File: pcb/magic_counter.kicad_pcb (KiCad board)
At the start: 2 copper layers, 127.4 x 152.4 mm, 30 parts, among them J1 ISP-Port, Q1 2SA1015, Q2 2SA1015, Q3 2SA1015, Q4 2SA1015, Q5 2SA1015, U1 ATmega32A-P, U2 74HC595, U7 LTC-4627JF, Y1 Crystal

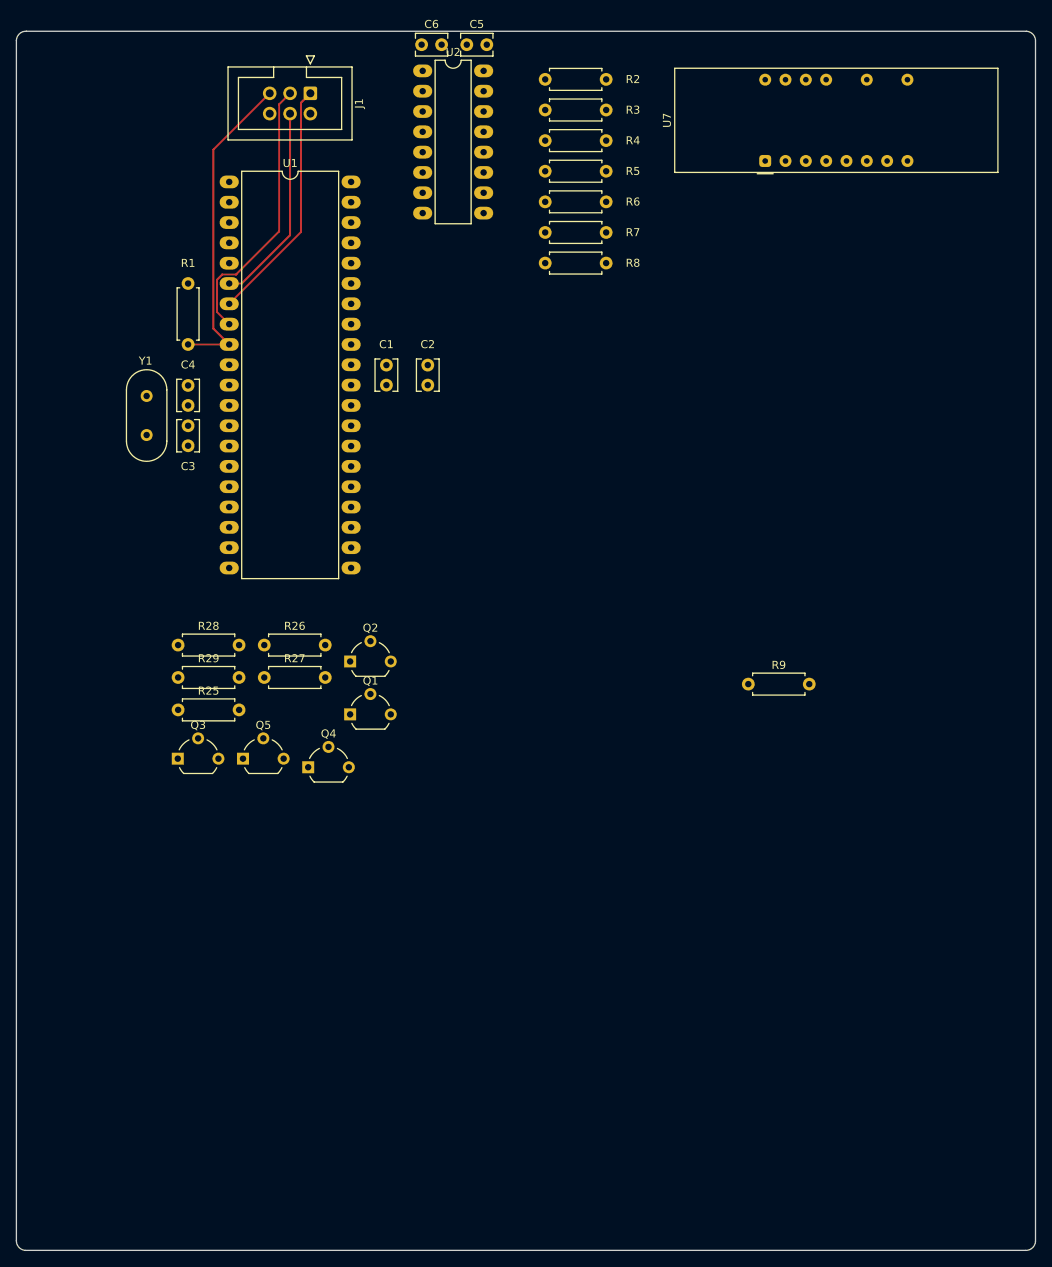
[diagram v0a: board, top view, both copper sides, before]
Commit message: test layout and first traces
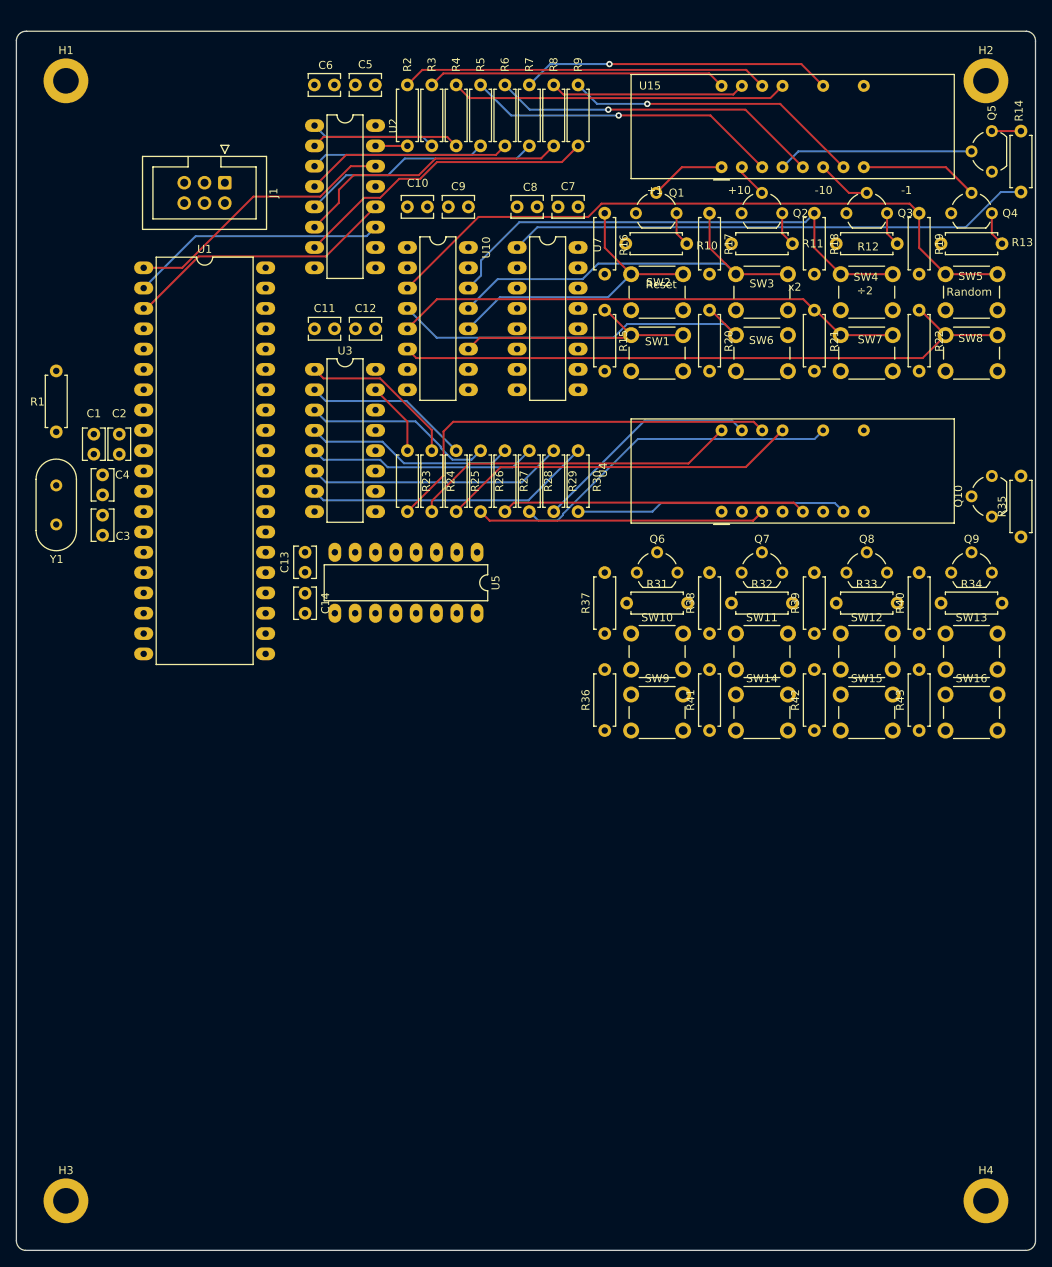
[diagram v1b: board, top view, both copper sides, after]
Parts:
- added C10: 1nF, Capacitor_THT:C_Disc_D3.8mm_W2.6mm_P2.50mm, F.Cu at (83.1, 45.6)
- added C11: 100pF, Capacitor_THT:C_Disc_D3.8mm_W2.6mm_P2.50mm, F.Cu at (69.0, 60.8)
- added C12: 1nF, Capacitor_THT:C_Disc_D3.8mm_W2.6mm_P2.50mm, F.Cu at (74.1, 60.8)
- added C13: 100pF, Capacitor_THT:C_Disc_D3.8mm_W2.6mm_P2.50mm, F.Cu at (67.8, 91.3)
- added C14: 1nF, Capacitor_THT:C_Disc_D3.8mm_W2.6mm_P2.50mm, F.Cu at (67.8, 93.9)
- added C7: 100pF, Capacitor_THT:C_Disc_D3.8mm_W2.6mm_P2.50mm, F.Cu at (99.4, 45.6)
- added C8: 1nF, Capacitor_THT:C_Disc_D3.8mm_W2.6mm_P2.50mm, F.Cu at (96.8, 45.6)
- added C9: 100pF, Capacitor_THT:C_Disc_D3.8mm_W2.6mm_P2.50mm, F.Cu at (85.7, 45.6)
- added H1: MountingHole_Pad, MountingHole:MountingHole_3.2mm_M3_DIN965_Pad, F.Cu at (37.9, 29.8)
- added H2: MountingHole_Pad, MountingHole:MountingHole_3.2mm_M3_DIN965_Pad, F.Cu at (152.9, 29.8)
- added H3: MountingHole_Pad, MountingHole:MountingHole_3.2mm_M3_DIN965_Pad, F.Cu at (37.9, 169.8)
- added H4: MountingHole_Pad, MountingHole:MountingHole_3.2mm_M3_DIN965_Pad, F.Cu at (152.9, 169.8)
- added Q10: 2SA1015, Package_TO_SOT_THT:TO-92_Wide, F.Cu at (153.6, 84.3)
- added Q6: 2SA1015, Package_TO_SOT_THT:TO-92_Wide, F.Cu at (109.2, 91.3)
- added Q7: 2SA1015, Package_TO_SOT_THT:TO-92_Wide, F.Cu at (122.3, 91.3)
- added Q8: 2SA1015, Package_TO_SOT_THT:TO-92_Wide, F.Cu at (135.4, 91.3)
- added Q9: 2SA1015, Package_TO_SOT_THT:TO-92_Wide, F.Cu at (148.6, 91.3)
- added R10: 4.7k, Resistor_THT:R_Axial_DIN0207_L6.3mm_D2.5mm_P7.62mm_Horizontal, F.Cu at (107.9, 50.2)
- added R11: 4.7k, Resistor_THT:R_Axial_DIN0207_L6.3mm_D2.5mm_P7.62mm_Horizontal, F.Cu at (121.1, 50.2)
- added R12: 4.7k, Resistor_THT:R_Axial_DIN0207_L6.3mm_D2.5mm_P7.62mm_Horizontal, F.Cu at (134.2, 50.2)
- added R13: 4.7k, Resistor_THT:R_Axial_DIN0207_L6.3mm_D2.5mm_P7.62mm_Horizontal, F.Cu at (147.3, 50.2)
- added R14: 4.7k, Resistor_THT:R_Axial_DIN0207_L6.3mm_D2.5mm_P7.62mm_Horizontal, F.Cu at (157.3, 43.8)
- added R15: 10k, Resistor_THT:R_Axial_DIN0207_L6.3mm_D2.5mm_P7.62mm_Horizontal, F.Cu at (105.2, 66.1)
- added R16: 10k, Resistor_THT:R_Axial_DIN0207_L6.3mm_D2.5mm_P7.62mm_Horizontal, F.Cu at (105.2, 54.0)
- added R17: 10k, Resistor_THT:R_Axial_DIN0207_L6.3mm_D2.5mm_P7.62mm_Horizontal, F.Cu at (118.3, 54.0)
- added R18: 10k, Resistor_THT:R_Axial_DIN0207_L6.3mm_D2.5mm_P7.62mm_Horizontal, F.Cu at (131.4, 54.0)
- added R19: 10k, Resistor_THT:R_Axial_DIN0207_L6.3mm_D2.5mm_P7.62mm_Horizontal, F.Cu at (144.5, 54.0)
- added R20: 10k, Resistor_THT:R_Axial_DIN0207_L6.3mm_D2.5mm_P7.62mm_Horizontal, F.Cu at (118.3, 66.1)
- added R21: 10k, Resistor_THT:R_Axial_DIN0207_L6.3mm_D2.5mm_P7.62mm_Horizontal, F.Cu at (131.4, 66.1)
- added R22: 10k, Resistor_THT:R_Axial_DIN0207_L6.3mm_D2.5mm_P7.62mm_Horizontal, F.Cu at (144.5, 66.1)
- added R23: 100R, Resistor_THT:R_Axial_DIN0207_L6.3mm_D2.5mm_P7.62mm_Horizontal, F.Cu at (80.6, 76.1)
- added R24: 100R, Resistor_THT:R_Axial_DIN0207_L6.3mm_D2.5mm_P7.62mm_Horizontal, F.Cu at (83.6, 76.1)
- added R30: 100R, Resistor_THT:R_Axial_DIN0207_L6.3mm_D2.5mm_P7.62mm_Horizontal, F.Cu at (101.9, 76.1)
- added R31: 4.7k, Resistor_THT:R_Axial_DIN0207_L6.3mm_D2.5mm_P7.62mm_Horizontal, F.Cu at (108.0, 95.1)
- added R32: 4.7k, Resistor_THT:R_Axial_DIN0207_L6.3mm_D2.5mm_P7.62mm_Horizontal, F.Cu at (121.1, 95.1)
- added R33: 4.7k, Resistor_THT:R_Axial_DIN0207_L6.3mm_D2.5mm_P7.62mm_Horizontal, F.Cu at (134.2, 95.1)
- added R34: 4.7k, Resistor_THT:R_Axial_DIN0207_L6.3mm_D2.5mm_P7.62mm_Horizontal, F.Cu at (147.3, 95.1)
- added R35: 4.7k, Resistor_THT:R_Axial_DIN0207_L6.3mm_D2.5mm_P7.62mm_Horizontal, F.Cu at (157.3, 86.9)
- added R36: 10k, Resistor_THT:R_Axial_DIN0207_L6.3mm_D2.5mm_P7.62mm_Horizontal, F.Cu at (105.2, 111.1)
- added R37: 10k, Resistor_THT:R_Axial_DIN0207_L6.3mm_D2.5mm_P7.62mm_Horizontal, F.Cu at (105.2, 98.9)
- added R38: 10k, Resistor_THT:R_Axial_DIN0207_L6.3mm_D2.5mm_P7.62mm_Horizontal, F.Cu at (118.3, 98.9)
- added R39: 10k, Resistor_THT:R_Axial_DIN0207_L6.3mm_D2.5mm_P7.62mm_Horizontal, F.Cu at (131.4, 98.9)
- added R40: 10k, Resistor_THT:R_Axial_DIN0207_L6.3mm_D2.5mm_P7.62mm_Horizontal, F.Cu at (144.5, 98.9)
- added R41: 10k, Resistor_THT:R_Axial_DIN0207_L6.3mm_D2.5mm_P7.62mm_Horizontal, F.Cu at (118.3, 111.1)
- added R42: 10k, Resistor_THT:R_Axial_DIN0207_L6.3mm_D2.5mm_P7.62mm_Horizontal, F.Cu at (131.4, 111.1)
- added R43: 10k, Resistor_THT:R_Axial_DIN0207_L6.3mm_D2.5mm_P7.62mm_Horizontal, F.Cu at (144.5, 111.1)
- added SW1: Reset, Button_Switch_THT:SW_PUSH_6mm_H5mm, F.Cu at (108.5, 61.6)
- added SW10: +1, Button_Switch_THT:SW_PUSH_6mm_H5mm, F.Cu at (108.5, 98.9)
- added SW11: +10, Button_Switch_THT:SW_PUSH_6mm_H5mm, F.Cu at (121.6, 98.9)
- added SW12: -10, Button_Switch_THT:SW_PUSH_6mm_H5mm, F.Cu at (134.7, 98.9)
- added SW13: -1, Button_Switch_THT:SW_PUSH_6mm_H5mm, F.Cu at (147.8, 98.9)
- added SW14: x2, Button_Switch_THT:SW_PUSH_6mm_H5mm, F.Cu at (121.6, 106.6)
- added SW15: /2, Button_Switch_THT:SW_PUSH_6mm_H5mm, F.Cu at (134.7, 106.6)
- added SW16: Random, Button_Switch_THT:SW_PUSH_6mm_H5mm, F.Cu at (147.8, 106.6)
- added SW2: +1, Button_Switch_THT:SW_PUSH_6mm_H5mm, F.Cu at (108.5, 54.0)
- added SW3: +10, Button_Switch_THT:SW_PUSH_6mm_H5mm, F.Cu at (121.6, 54.0)
- added SW4: -10, Button_Switch_THT:SW_PUSH_6mm_H5mm, F.Cu at (134.7, 54.0)
- added SW5: -1, Button_Switch_THT:SW_PUSH_6mm_H5mm, F.Cu at (147.8, 54.0)
- added SW6: x2, Button_Switch_THT:SW_PUSH_6mm_H5mm, F.Cu at (121.6, 61.6)
- added SW7: /2, Button_Switch_THT:SW_PUSH_6mm_H5mm, F.Cu at (134.7, 61.6)
- added SW8: Random, Button_Switch_THT:SW_PUSH_6mm_H5mm, F.Cu at (147.8, 61.6)
- added SW9: Reset, Button_Switch_THT:SW_PUSH_6mm_H5mm, F.Cu at (108.5, 106.6)
- added U10: 74HC165, Package_DIP:DIP-16_W7.62mm_LongPads, F.Cu at (80.6, 50.7)
- added U15: LTC-4627JF, Display_7Segment:LTC-4627Jx, F.Cu at (119.8, 40.6)
- added U3: 74HC595, Package_DIP:DIP-16_W7.62mm_LongPads, F.Cu at (69.0, 65.9)
- added U4: LTC-4627JF, Display_7Segment:LTC-4627Jx, F.Cu at (119.8, 83.7)
- added U5: 74HC165, Package_DIP:DIP-16_W7.62mm_LongPads, F.Cu at (89.3, 88.8)
- R25, R26, R27, R28, R29: value 4.7k -> 100R
- U7: value LTC-4627JF -> 4028; footprint Display_7Segment:LTC-4627Jx -> Package_DIP:DIP-16_W7.62mm_LongPads
- moved Q5 118.9 mm to (153.6, 41.2), turned to 90 degrees
- moved Q3 107.9 mm to (135.4, 46.4)
- moved Q4 106.1 mm to (148.6, 46.4)
- moved Q2 74.4 mm to (122.3, 46.4)
- moved Q1 72.1 mm to (109.1, 46.4)
- moved R9 70.6 mm to (101.9, 38.0), turned to 90 degrees
- moved R29 54.8 mm to (98.9, 76.1), turned to -90 degrees
- moved R28 50.2 mm to (95.8, 76.1), turned to -90 degrees
- moved R25 47.5 mm to (86.7, 76.1), turned to -90 degrees
- moved R27 41.3 mm to (92.8, 76.1), turned to -90 degrees
- moved C2 39.5 mm to (44.6, 76.5)
- moved C1 37.6 mm to (41.4, 76.5)
- moved R26 36.4 mm to (89.7, 76.1), turned to -90 degrees
- moved U7 32.8 mm to (94.3, 50.7), turned to 0 degrees
- moved R2 19.1 mm to (80.6, 38.0), turned to 90 degrees
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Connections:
- R25 pad 1: unconnected-(R25-Pad1) -> Net-(R25-Pad1)
- R25 pad 2: Net-(Q1-Pad3) -> Net-(R25-Pad2)
- R26 pad 1: unconnected-(R26-Pad1) -> Net-(R26-Pad1)
- R26 pad 2: Net-(Q2-Pad3) -> Net-(R26-Pad2)
- R27 pad 1: unconnected-(R27-Pad1) -> Net-(R27-Pad1)
- R27 pad 2: Net-(Q3-Pad3) -> Net-(R27-Pad2)
- R28 pad 1: unconnected-(R28-Pad1) -> Net-(R28-Pad1)
- R28 pad 2: Net-(Q4-Pad3) -> Net-(R28-Pad2)
- R29 pad 1: unconnected-(R29-Pad1) -> Net-(R29-Pad1)
- R29 pad 2: Net-(Q5-Pad3) -> Net-(R29-Pad2)
- U1 pad 1: unconnected-(U1-Pad1) -> /PB1
- U1 pad 14: unconnected-(U1-Pad14) -> /PD0
- U1 pad 15: unconnected-(U1-Pad15) -> /PD1
- U1 pad 16: unconnected-(U1-Pad16) -> /PD2
- U1 pad 17: unconnected-(U1-Pad17) -> /PD3
- U1 pad 2: unconnected-(U1-Pad2) -> /PB2
- U1 pad 3: unconnected-(U1-Pad3) -> /PB3
- U1 pad 37: unconnected-(U1-Pad37) -> /PA3
- U1 pad 38: unconnected-(U1-Pad38) -> /PA2
- U1 pad 39: unconnected-(U1-Pad39) -> /PA1
- U1 pad 40: unconnected-(U1-Pad40) -> /PA0
- U2 pad 10: unconnected-(U2-Pad10) -> +5V
- U2 pad 11: unconnected-(U2-Pad11) -> /PB2
- U2 pad 12: unconnected-(U2-Pad12) -> /PB3
- U2 pad 13: unconnected-(U2-Pad13) -> GND
- U2 pad 14: unconnected-(U2-Pad14) -> /PB1
- U2 pad 9: unconnected-(U2-Pad9) -> /Display_life/2nd_Bitshifter
- U7 pad 1: Net-(Q1-Pad2) -> /Display_life/D1_CA5
- U7 pad 11: Net-(R7-Pad2) -> /PA3
- U7 pad 13: Net-(R4-Pad2) -> /PA1
- U7 pad 14: Net-(R2-Pad2) -> /Display_life/D1_CA2
- U7 pad 15: Net-(R8-Pad2) -> /Display_life/D1_CA4
- U7 pad 16: Net-(R3-Pad2) -> +5V
- U7 pad 2: Net-(Q2-Pad2) -> /Display_life/D1_CA3
- U7 pad 3: Net-(R5-Pad2) -> /Display_life/D1_CA1
- U7 pad 4: Net-(Q5-Pad2) -> /Display_life/D2_CA3
- U7 pad 5: Net-(R6-Pad2) -> /Display_life/D2_CA5
- U7 pad 6: Net-(Q3-Pad2) -> /Display_life/D2_CA1
- U7 pad 7: Net-(R9-Pad2) -> /Display_life/D2_CA2
- U7 pad 8: Net-(Q4-Pad2) -> GND
- U7 pad 9: unconnected-(U7-Pad9) -> /Display_life/D2_CA4
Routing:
- net Net-(R19-Pad2): track 0.00 -> 84.3 mm
- net Net-(R22-Pad2): track 0.00 -> 80.0 mm
- net /Display_life/D1_CA5: track 0.00 -> 65.9 mm
- net Net-(R21-Pad2): track 0.00 -> 64.1 mm
- net Net-(R18-Pad2): track 0.00 -> 63.7 mm
- net Net-(R23-Pad2): track 0.00 -> 52.7 mm
- net Net-(R17-Pad2): track 0.00 -> 51.8 mm
- net Net-(R20-Pad2): track 0.00 -> 48.5 mm
- net Net-(R2-Pad2): track 0.00 -> 46.0 mm
- net Net-(R25-Pad2): track 0.00 -> 45.0 mm
- net Net-(R4-Pad2): track 0.00 -> 42.1 mm
- net Net-(R28-Pad2): track 0.00 -> 42.0 mm
- net Net-(R6-Pad2): track 0.00 -> 41.5 mm, vias 0 -> 1
- net Net-(R24-Pad2): track 0.00 -> 41.2 mm
- net /Reset: track 40.3 -> 0.00 mm
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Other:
- board text added: "+1"
- board text added: "+10"
- board text added: "-1"
- board text added: "-10"
- board text added: "Random"
- board text added: "Reset"
- board text added: "x2"
- board text added: "÷2"

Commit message: new layout test
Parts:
- added C15: ~, Capacitor_THT:C_Disc_D3.8mm_W2.6mm_P2.50mm, F.Cu at (439.0, 172.1)
- added C16: ~, Capacitor_THT:C_Disc_D3.8mm_W2.6mm_P2.50mm, F.Cu at (449.6, 163.5)
- added C17: ~, Capacitor_THT:C_Disc_D3.8mm_W2.6mm_P2.50mm, F.Cu at (417.5, 197.7)
- added C18: ~, Capacitor_THT:C_Disc_D3.8mm_W2.6mm_P2.50mm, F.Cu at (396.2, 204.9)
- added C19: 100pF, Capacitor_THT:C_Disc_D3.8mm_W2.6mm_P2.50mm, F.Cu at (440.8, 112.8)
- added C20: 1nF, Capacitor_THT:C_Disc_D3.8mm_W2.6mm_P2.50mm, F.Cu at (433.1, 119.4)
- added C21: 100pF, Capacitor_THT:C_Disc_D3.8mm_W2.6mm_P2.50mm, F.Cu at (448.9, 102.2)
- added C22: 1nF, Capacitor_THT:C_Disc_D3.8mm_W2.6mm_P2.50mm, F.Cu at (427.5, 123.6)
- added C23: 100pF, Capacitor_THT:C_Disc_D3.8mm_W2.6mm_P2.50mm, F.Cu at (421.8, 118.4)
- added C24: 1nF, Capacitor_THT:C_Disc_D3.8mm_W2.6mm_P2.50mm, F.Cu at (427.5, 119.4)
- added Q11: 2SA1015, Package_TO_SOT_THT:TO-92_Wide, F.Cu at (419.3, 132.7)
- added Q12: 2SA1015, Package_TO_SOT_THT:TO-92_Wide, F.Cu at (409.4, 140.8)
- added Q13: 2SA1015, Package_TO_SOT_THT:TO-92_Wide, F.Cu at (408.5, 134.2)
- added Q14: 2SA1015, Package_TO_SOT_THT:TO-92_Wide, F.Cu at (432.6, 108.2)
- added Q15: 2SA1015, Package_TO_SOT_THT:TO-92_Wide, F.Cu at (419.3, 126.1)
- added Q16: 2SA1015, Package_TO_SOT_THT:TO-92_Wide, F.Cu at (398.6, 150.4)
- added Q17: 2SA1015, Package_TO_SOT_THT:TO-92_Wide, F.Cu at (401.3, 142.3)
- added Q18: 2SA1015, Package_TO_SOT_THT:TO-92_Wide, F.Cu at (432.6, 114.8)
- added Q19: 2SA1015, Package_TO_SOT_THT:TO-92_Wide, F.Cu at (440.7, 108.2)
- added Q20: 2SA1015, Package_TO_SOT_THT:TO-92_Wide, F.Cu at (390.5, 150.4)
- added R44: 10k, Resistor_THT:R_Axial_DIN0207_L6.3mm_D2.5mm_P7.62mm_Horizontal, F.Cu at (385.6, 163.5)
- added R45: 10k, Resistor_THT:R_Axial_DIN0207_L6.3mm_D2.5mm_P7.62mm_Horizontal, F.Cu at (385.6, 167.5)
- added R46: 10k, Resistor_THT:R_Axial_DIN0207_L6.3mm_D2.5mm_P7.62mm_Horizontal, F.Cu at (385.6, 183.7)
- added R47: 10k, Resistor_THT:R_Axial_DIN0207_L6.3mm_D2.5mm_P7.62mm_Horizontal, F.Cu at (385.6, 179.7)
- added R48: 10k, Resistor_THT:R_Axial_DIN0207_L6.3mm_D2.5mm_P7.62mm_Horizontal, F.Cu at (396.4, 171.6)
- added R49: 10k, Resistor_THT:R_Axial_DIN0207_L6.3mm_D2.5mm_P7.62mm_Horizontal, F.Cu at (396.4, 179.7)
- added R50: 10k, Resistor_THT:R_Axial_DIN0207_L6.3mm_D2.5mm_P7.62mm_Horizontal, F.Cu at (407.2, 171.6)
- added R51: 10k, Resistor_THT:R_Axial_DIN0207_L6.3mm_D2.5mm_P7.62mm_Horizontal, F.Cu at (385.6, 175.6)
- added R52: 10k, Resistor_THT:R_Axial_DIN0207_L6.3mm_D2.5mm_P7.62mm_Horizontal, F.Cu at (396.4, 167.5)
- added R53: 10k, Resistor_THT:R_Axial_DIN0207_L6.3mm_D2.5mm_P7.62mm_Horizontal, F.Cu at (407.2, 163.5)
- added R54: 10k, Resistor_THT:R_Axial_DIN0207_L6.3mm_D2.5mm_P7.62mm_Horizontal, F.Cu at (396.4, 183.7)
- added R55: 10k, Resistor_THT:R_Axial_DIN0207_L6.3mm_D2.5mm_P7.62mm_Horizontal, F.Cu at (396.4, 163.5)
- added R56: 10k, Resistor_THT:R_Axial_DIN0207_L6.3mm_D2.5mm_P7.62mm_Horizontal, F.Cu at (385.6, 171.6)
- added R57: 10k, Resistor_THT:R_Axial_DIN0207_L6.3mm_D2.5mm_P7.62mm_Horizontal, F.Cu at (385.6, 187.8)
- added R58: 10k, Resistor_THT:R_Axial_DIN0207_L6.3mm_D2.5mm_P7.62mm_Horizontal, F.Cu at (396.4, 175.6)
- added R59: 10k, Resistor_THT:R_Axial_DIN0207_L6.3mm_D2.5mm_P7.62mm_Horizontal, F.Cu at (407.2, 167.5)
- added R60: 4.7k, Resistor_THT:R_Axial_DIN0207_L6.3mm_D2.5mm_P7.62mm_Horizontal, F.Cu at (369.0, 143.8)
- added R61: 4.7k, Resistor_THT:R_Axial_DIN0207_L6.3mm_D2.5mm_P7.62mm_Horizontal, F.Cu at (358.2, 143.8)
- added R62: 4.7k, Resistor_THT:R_Axial_DIN0207_L6.3mm_D2.5mm_P7.62mm_Horizontal, F.Cu at (397.8, 136.2)
- added R63: 4.7k, Resistor_THT:R_Axial_DIN0207_L6.3mm_D2.5mm_P7.62mm_Horizontal, F.Cu at (397.8, 128.1)
- added R64: 4.7k, Resistor_THT:R_Axial_DIN0207_L6.3mm_D2.5mm_P7.62mm_Horizontal, F.Cu at (387.0, 132.1)
- added R65: 4.7k, Resistor_THT:R_Axial_DIN0207_L6.3mm_D2.5mm_P7.62mm_Horizontal, F.Cu at (421.8, 102.1)
- added R66: 4.7k, Resistor_THT:R_Axial_DIN0207_L6.3mm_D2.5mm_P7.62mm_Horizontal, F.Cu at (379.8, 147.9)
- added R67: 100R, Resistor_THT:R_Axial_DIN0207_L6.3mm_D2.5mm_P7.62mm_Horizontal, F.Cu at (432.6, 102.1)
- added R68: 100R, Resistor_THT:R_Axial_DIN0207_L6.3mm_D2.5mm_P7.62mm_Horizontal, F.Cu at (369.0, 151.9)
- added R69: 100R, Resistor_THT:R_Axial_DIN0207_L6.3mm_D2.5mm_P7.62mm_Horizontal, F.Cu at (421.8, 114.3)
- added R70: 100R, Resistor_THT:R_Axial_DIN0207_L6.3mm_D2.5mm_P7.62mm_Horizontal, F.Cu at (387.0, 136.2)
- added R71: 100R, Resistor_THT:R_Axial_DIN0207_L6.3mm_D2.5mm_P7.62mm_Horizontal, F.Cu at (358.2, 151.9)
- added R72: 4.7k, Resistor_THT:R_Axial_DIN0207_L6.3mm_D2.5mm_P7.62mm_Horizontal, F.Cu at (408.6, 124.0)
- added R73: 100R, Resistor_THT:R_Axial_DIN0207_L6.3mm_D2.5mm_P7.62mm_Horizontal, F.Cu at (421.8, 110.2)
- added R74: 100R, Resistor_THT:R_Axial_DIN0207_L6.3mm_D2.5mm_P7.62mm_Horizontal, F.Cu at (397.8, 132.1)
- added R75: 100R, Resistor_THT:R_Axial_DIN0207_L6.3mm_D2.5mm_P7.62mm_Horizontal, F.Cu at (387.0, 124.0)
- added R76: 4.7k, Resistor_THT:R_Axial_DIN0207_L6.3mm_D2.5mm_P7.62mm_Horizontal, F.Cu at (390.5, 144.3)
- added R77: 4.7k, Resistor_THT:R_Axial_DIN0207_L6.3mm_D2.5mm_P7.62mm_Horizontal, F.Cu at (369.0, 147.9)
- added R78: 100R, Resistor_THT:R_Axial_DIN0207_L6.3mm_D2.5mm_P7.62mm_Horizontal, F.Cu at (379.8, 151.9)
- added R79: 100R, Resistor_THT:R_Axial_DIN0207_L6.3mm_D2.5mm_P7.62mm_Horizontal, F.Cu at (358.2, 147.9)
- added R80: 100R, Resistor_THT:R_Axial_DIN0207_L6.3mm_D2.5mm_P7.62mm_Horizontal, F.Cu at (390.5, 140.2)
- added R81: 100R, Resistor_THT:R_Axial_DIN0207_L6.3mm_D2.5mm_P7.62mm_Horizontal, F.Cu at (408.6, 128.1)
- added R82: 100R, Resistor_THT:R_Axial_DIN0207_L6.3mm_D2.5mm_P7.62mm_Horizontal, F.Cu at (397.8, 124.0)
- added R83: 100R, Resistor_THT:R_Axial_DIN0207_L6.3mm_D2.5mm_P7.62mm_Horizontal, F.Cu at (387.0, 128.1)
- added R84: 100R, Resistor_THT:R_Axial_DIN0207_L6.3mm_D2.5mm_P7.62mm_Horizontal, F.Cu at (379.8, 143.8)
- added R85: 100R, Resistor_THT:R_Axial_DIN0207_L6.3mm_D2.5mm_P7.62mm_Horizontal, F.Cu at (421.8, 106.2)
- added SW17: ~, Button_Switch_THT:SW_PUSH_6mm_H5mm, F.Cu at (418.4, 163.5)
- added SW18: ~, Button_Switch_THT:SW_PUSH_6mm_H5mm, F.Cu at (428.9, 163.5)
- added SW19: ~, Button_Switch_THT:SW_PUSH_6mm_H5mm, F.Cu at (418.4, 172.0)
- added SW20: ~, Button_Switch_THT:SW_PUSH_6mm_H5mm, F.Cu at (407.2, 201.3)
- added SW21: ~, Button_Switch_THT:SW_PUSH_6mm_H5mm, F.Cu at (407.6, 184.2)
- added SW22: ~, Button_Switch_THT:SW_PUSH_6mm_H5mm, F.Cu at (439.5, 163.5)
- added SW23: ~, Button_Switch_THT:SW_PUSH_6mm_H5mm, F.Cu at (407.4, 192.7)
- added SW24: ~, Button_Switch_THT:SW_PUSH_6mm_H5mm, F.Cu at (386.1, 191.8)
- added SW25: ~, Button_Switch_THT:SW_PUSH_6mm_H5mm, F.Cu at (428.9, 172.0)
- added SW26: ~, Button_Switch_THT:SW_PUSH_6mm_H5mm, F.Cu at (396.6, 196.3)
- added SW27: ~, Button_Switch_THT:SW_PUSH_6mm_H5mm, F.Cu at (428.7, 180.6)
- added SW28: ~, Button_Switch_THT:SW_PUSH_6mm_H5mm, F.Cu at (396.8, 187.8)
- added SW29: ~, Button_Switch_THT:SW_PUSH_6mm_H5mm, F.Cu at (418.2, 180.6)
- added SW30: ~, Button_Switch_THT:SW_PUSH_6mm_H5mm, F.Cu at (418.2, 189.1)
- added SW31: ~, Button_Switch_THT:SW_PUSH_6mm_H5mm, F.Cu at (386.1, 200.4)
- added SW32: ~, Button_Switch_THT:SW_PUSH_6mm_H5mm, F.Cu at (407.6, 175.6)
- added U11: 4028, Package_DIP:DIP-16_W7.62mm_LongPads, F.Cu at (399.0, 102.2)
- added U12: LTC-4627JF, Display_7Segment:LTC-4627Jx, F.Cu at (358.8, 112.1)
- added U13: LTC-4627JF, Display_7Segment:LTC-4627Jx, F.Cu at (410.6, 102.2)
- added U14: ~, Package_DIP:DIP-16_W7.62mm_LongPads, F.Cu at (373.2, 112.1)
- added U6: LTC-4627JF, Display_7Segment:LTC-4627Jx, F.Cu at (55.3, 88.9)
- added U8: 74HC165, Package_DIP:DIP-16_W7.62mm_LongPads, F.Cu at (201.2, 58.9)
- added U9: 74HC595, Package_DIP:DIP-16_W7.62mm_LongPads, F.Cu at (387.4, 102.2)
- U10: value 74HC165 -> 74HC595
- U15: value LTC-4627JF -> ~; footprint Display_7Segment:LTC-4627Jx -> Package_DIP:DIP-16_W7.62mm_LongPads
- U4: value LTC-4627JF -> 4028; footprint Display_7Segment:LTC-4627Jx -> Package_DIP:DIP-16_W7.62mm_LongPads
- U5: value 74HC165 -> LTC-4627JF; footprint Package_DIP:DIP-16_W7.62mm_LongPads -> Display_7Segment:LTC-4627Jx
- U7: value 4028 -> 74HC165
- moved U15 389.6 mm to (492.5, 154.2)
- moved U10 306.9 mm to (383.2, -0.31)
- moved C13 306.9 mm to (370.4, 40.3)
- moved C14 306.9 mm to (370.4, 42.9)
- moved R40 141.1 mm to (275.3, 151.9)
- moved SW13 123.7 mm to (263.1, 143.8)
- moved SW14 123.7 mm to (236.9, 151.5)
- moved R41 123.7 mm to (233.6, 156.0)
- moved R42 123.7 mm to (246.7, 156.0)
- moved R43 123.7 mm to (259.8, 156.0)
- moved SW15 123.7 mm to (250.0, 151.5)
- moved SW16 123.7 mm to (263.1, 151.5)
- moved SW5 110.3 mm to (37.6, 59.4)
- moved Y1 105.0 mm to (130.6, 127.4), turned to 90 degrees
- moved R19 97.9 mm to (47.5, 67.0)
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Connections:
- U1 pad 33: unconnected-(U1-Pad33) -> /PA7
- U1 pad 34: unconnected-(U1-Pad34) -> /PA6
- U1 pad 35: unconnected-(U1-Pad35) -> /PA5
- U1 pad 36: unconnected-(U1-Pad36) -> /PA4
- U10 pad 1: /PD1 -> Net-(R79-Pad1)
- U10 pad 10: /Buttons/Serial_2 -> +5V
- U10 pad 11: Net-(R15-Pad2) -> /PB2
- U10 pad 12: Net-(R16-Pad2) -> /PB3
- U10 pad 13: Net-(R17-Pad2) -> GND
- U10 pad 14: Net-(R18-Pad2) -> /Display_3_and_4/4th_Bitshifter
- U10 pad 15: /PD2 -> Net-(R78-Pad1)
- U10 pad 2: /PD0 -> Net-(R80-Pad1)
- U10 pad 3: Net-(R19-Pad2) -> Net-(R81-Pad1)
- U10 pad 4: Net-(R20-Pad2) -> Net-(R82-Pad1)
- U10 pad 5: Net-(R21-Pad2) -> Net-(R83-Pad1)
- U10 pad 6: Net-(R22-Pad2) -> Net-(R84-Pad1)
- U10 pad 7: GND -> Net-(R85-Pad1)
- U10 pad 9: /PD3 -> unconnected-(U10-Pad9)
- U15 pad 1: Net-(Q1-Pad2) -> /PD1
- U15 pad 11: Net-(R7-Pad2) -> Net-(R52-Pad2)
- U15 pad 13: Net-(R4-Pad2) -> Net-(R54-Pad2)
- U15 pad 14: Net-(R2-Pad2) -> Net-(R55-Pad2)
- U15 pad 15: Net-(R8-Pad2) -> /PD2
- U15 pad 16: Net-(R3-Pad2) -> +5V
- U15 pad 2: Net-(Q2-Pad2) -> /PD0
- U15 pad 3: Net-(R5-Pad2) -> Net-(R56-Pad2)
- U15 pad 4: Net-(Q5-Pad2) -> Net-(R57-Pad2)
- U15 pad 5: Net-(R6-Pad2) -> Net-(R58-Pad2)
- U15 pad 6: Net-(Q3-Pad2) -> Net-(R59-Pad2)
- U15 pad 7: Net-(R9-Pad2) -> GND
- U15 pad 8: Net-(Q4-Pad2) -> GND
- U15 pad 9: unconnected-(U15-Pad9) -> /Buttons_Row_3_and_4/Serial_4
- U3 pad 9: /Display_life/3rd_Bitshifter -> /next_bitshifter
- U4 pad 1: Net-(Q6-Pad2) -> /Display_life/D1_CA5
- U4 pad 11: Net-(R28-Pad2) -> /PA3
- U4 pad 13: Net-(R25-Pad2) -> /PA1
- U4 pad 14: Net-(R23-Pad2) -> /Display_life/D1_CA2
- U4 pad 15: Net-(R29-Pad2) -> /Display_life/D1_CA4
- U4 pad 16: Net-(R24-Pad2) -> +5V
- U4 pad 2: Net-(Q7-Pad2) -> /Display_life/D1_CA3
- U4 pad 3: Net-(R26-Pad2) -> /Display_life/D1_CA1
- U4 pad 4: Net-(Q10-Pad2) -> /Display_life/D2_CA3
- U4 pad 5: Net-(R27-Pad2) -> /Display_life/D2_CA5
- U4 pad 6: Net-(Q8-Pad2) -> /Display_life/D2_CA1
- U4 pad 7: Net-(R30-Pad2) -> /Display_life/D2_CA2
- U4 pad 8: Net-(Q9-Pad2) -> GND
- U4 pad 9: unconnected-(U4-Pad9) -> /Display_life/D2_CA4
- U5 pad 1: /PD1 -> Net-(Q1-Pad2)
- U5 pad 11: Net-(R36-Pad2) -> Net-(R7-Pad2)
- U5 pad 13: Net-(R38-Pad2) -> Net-(R4-Pad2)
- U5 pad 14: Net-(R39-Pad2) -> Net-(R2-Pad2)
- U5 pad 15: /PD2 -> Net-(R8-Pad2)
- U5 pad 16: +5V -> Net-(R3-Pad2)
- U5 pad 2: /PD0 -> Net-(Q2-Pad2)
- U5 pad 3: Net-(R40-Pad2) -> Net-(R5-Pad2)
- U5 pad 4: Net-(R41-Pad2) -> Net-(Q5-Pad2)
- U5 pad 5: Net-(R42-Pad2) -> Net-(R6-Pad2)
- U5 pad 6: Net-(R43-Pad2) -> Net-(Q3-Pad2)
- U5 pad 7: GND -> Net-(R9-Pad2)
- U5 pad 8: GND -> Net-(Q4-Pad2)
- U5 pad 9: /Buttons/Serial_2 -> unconnected-(U5-Pad9)
- U7 pad 1: /Display_life/D1_CA5 -> /PD1
- U7 pad 10: /PA0 -> /Buttons_Row_1_and_2/Serial_2
- U7 pad 11: /PA3 -> Net-(R15-Pad2)
- U7 pad 12: /PA2 -> Net-(R16-Pad2)
- U7 pad 13: /PA1 -> Net-(R17-Pad2)
- U7 pad 14: /Display_life/D1_CA2 -> Net-(R18-Pad2)
- U7 pad 15: /Display_life/D1_CA4 -> /PD2
- U7 pad 2: /Display_life/D1_CA3 -> /PD0
- U7 pad 3: /Display_life/D1_CA1 -> Net-(R19-Pad2)
- U7 pad 4: /Display_life/D2_CA3 -> Net-(R20-Pad2)
- U7 pad 5: /Display_life/D2_CA5 -> Net-(R21-Pad2)
- U7 pad 6: /Display_life/D2_CA1 -> Net-(R22-Pad2)
- U7 pad 7: /Display_life/D2_CA2 -> GND
- U7 pad 9: /Display_life/D2_CA4 -> /PD3
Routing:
- net Net-(R19-Pad2): track 84.3 -> 0.00 mm
- net Net-(R22-Pad2): track 80.0 -> 0.00 mm
- net /Display_life/D1_CA5: track 65.9 -> 0.00 mm
- net Net-(R21-Pad2): track 64.1 -> 0.00 mm
- net Net-(R18-Pad2): track 63.7 -> 0.00 mm
- net Net-(R23-Pad2): track 52.7 -> 0.00 mm
- net Net-(R17-Pad2): track 51.8 -> 0.00 mm
- net Net-(R20-Pad2): track 48.5 -> 0.00 mm
- net Net-(R2-Pad2): track 46.0 -> 0.00 mm
- net Net-(R25-Pad2): track 45.0 -> 0.00 mm
- net Net-(R4-Pad2): track 42.1 -> 0.00 mm
- net Net-(R28-Pad2): track 42.0 -> 0.00 mm
- net Net-(R6-Pad2): track 41.5 -> 0.00 mm, vias 1 -> 0
- net Net-(R24-Pad2): track 41.2 -> 0.00 mm
- net Net-(R5-Pad2): track 39.5 -> 0.00 mm, vias 1 -> 0
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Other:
- board size 127.4 x 152.4 mm -> 127.4 x 202.4 mm
- board text removed: "+1"
- board text removed: "+10"
- board text removed: "-1"
- board text removed: "-10"
- board text removed: "Random"
- board text removed: "Reset"
- board text removed: "x2"
- board text removed: "÷2"

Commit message: reassigned designators and layout progress
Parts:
- R60, R61, R62, R63, R64, R65, R66, R76, R77: value 4.7k -> 100R
- R68, R69, R70, R71, R81, R82, R83, R84, R85: value 100R -> 4.7k
- moved Q18 439.4 mm to (4.32, 213.4)
- moved U10 402.9 mm to (62.8, 243.9), turned to 90 degrees
- moved C23 396.4 mm to (44.7, 240.2)
- moved C24 396.4 mm to (50.3, 241.3)
- moved SW22 388.7 mm to (50.8, 170.4)
- moved SW17 380.8 mm to (37.6, 157.6)
- moved SW18 378.2 mm to (50.8, 157.6)
- moved SW21 370.2 mm to (37.6, 170.4)
- moved U13 364.9 mm to (57.7, 194.5), turned to 90 degrees
- moved C16 358.5 mm to (91.4, 180.1), turned to -90 degrees
- moved SW19 354.5 mm to (64.2, 157.6)
- moved C19 353.2 mm to (91.4, 165.1), turned to 90 degrees
- moved R48 348.9 mm to (47.5, 178.1), turned to 90 degrees
- moved C15 347.6 mm to (91.4, 177.4), turned to 90 degrees
- moved C20 345.2 mm to (91.4, 167.9), turned to -90 degrees
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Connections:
- R60 pad 1: /Display_3_and_4/D3_CA5 -> Net-(R60-Pad1)
- R60 pad 2: Net-(Q11-Pad3) -> Net-(R60-Pad2)
- R61 pad 1: /Display_3_and_4/D3_CA4 -> Net-(R61-Pad1)
- R61 pad 2: Net-(Q12-Pad3) -> Net-(R61-Pad2)
- R62 pad 1: /Display_3_and_4/D3_CA3 -> Net-(R62-Pad1)
- R62 pad 2: Net-(Q13-Pad3) -> Net-(R62-Pad2)
- R63 pad 1: /Display_3_and_4/D3_CA2 -> Net-(R63-Pad1)
- R63 pad 2: Net-(Q14-Pad3) -> Net-(R63-Pad2)
- R64 pad 1: /Display_3_and_4/D4_CA5 -> Net-(R64-Pad1)
- R64 pad 2: Net-(Q15-Pad3) -> Net-(R64-Pad2)
- R65 pad 1: /Display_3_and_4/D3_CA1 -> Net-(R65-Pad1)
- R65 pad 2: Net-(Q16-Pad3) -> Net-(R65-Pad2)
- R66 pad 1: /Display_3_and_4/D4_CA4 -> Net-(R66-Pad1)
- R66 pad 2: Net-(Q17-Pad3) -> Net-(R66-Pad2)
- R68 pad 1: Net-(R68-Pad1) -> /Display_3_and_4/D3_CA1
- R68 pad 2: Net-(R68-Pad2) -> Net-(Q15-Pad3)
- R69 pad 1: Net-(R69-Pad1) -> /Display_3_and_4/D3_CA2
- R69 pad 2: Net-(R69-Pad2) -> Net-(Q14-Pad3)
- R70 pad 1: Net-(R70-Pad1) -> /Display_3_and_4/D3_CA3
- R70 pad 2: Net-(R70-Pad2) -> Net-(Q13-Pad3)
- R71 pad 1: Net-(R71-Pad1) -> /Display_3_and_4/D3_CA4
- R71 pad 2: Net-(R71-Pad2) -> Net-(Q12-Pad3)
- R72 pad 1: /Display_3_and_4/D4_CA3 -> /Display_3_and_4/D3_CA5
- R72 pad 2: Net-(Q18-Pad3) -> Net-(Q11-Pad3)
- R76 pad 1: /Display_3_and_4/D4_CA2 -> Net-(R76-Pad1)
- R76 pad 2: Net-(Q19-Pad3) -> Net-(R76-Pad2)
- R77 pad 1: /Display_3_and_4/D4_CA1 -> Net-(R77-Pad1)
- R77 pad 2: Net-(Q20-Pad3) -> Net-(R77-Pad2)
- R81 pad 1: Net-(R81-Pad1) -> /Display_3_and_4/D4_CA1
- R81 pad 2: Net-(R81-Pad2) -> Net-(Q20-Pad3)
- R82 pad 1: Net-(R82-Pad1) -> /Display_3_and_4/D4_CA2
- R82 pad 2: Net-(R82-Pad2) -> Net-(Q19-Pad3)
- R83 pad 1: Net-(R83-Pad1) -> /Display_3_and_4/D4_CA3
- R83 pad 2: Net-(R83-Pad2) -> Net-(Q18-Pad3)
- R84 pad 1: Net-(R84-Pad1) -> /Display_3_and_4/D4_CA4
- R84 pad 2: Net-(R84-Pad2) -> Net-(Q17-Pad3)
- R85 pad 1: Net-(R85-Pad1) -> /Display_3_and_4/D4_CA5
- R85 pad 2: Net-(R85-Pad2) -> Net-(Q16-Pad3)
- U10 pad 1: Net-(R79-Pad1) -> Net-(R74-Pad1)
- U10 pad 15: Net-(R78-Pad1) -> Net-(R73-Pad1)
- U10 pad 2: Net-(R80-Pad1) -> Net-(R75-Pad1)
- U10 pad 3: Net-(R81-Pad1) -> Net-(R76-Pad1)
- U10 pad 4: Net-(R82-Pad1) -> Net-(R77-Pad1)
- U10 pad 5: Net-(R83-Pad1) -> Net-(R78-Pad1)
- U10 pad 6: Net-(R84-Pad1) -> Net-(R79-Pad1)
- U10 pad 7: Net-(R85-Pad1) -> Net-(R80-Pad1)
- U12 pad 1: Net-(Q16-Pad2) -> Net-(Q15-Pad2)
- U12 pad 11: Net-(R73-Pad2) -> Net-(R65-Pad2)
- U12 pad 13: Net-(R69-Pad2) -> Net-(R62-Pad2)
- U12 pad 14: Net-(R67-Pad2) -> Net-(R60-Pad2)
- U12 pad 15: Net-(R74-Pad2) -> Net-(R66-Pad2)
- U12 pad 16: Net-(R68-Pad2) -> Net-(R61-Pad2)
- U12 pad 3: Net-(R70-Pad2) -> Net-(R63-Pad2)
- U12 pad 5: Net-(R71-Pad2) -> Net-(R64-Pad2)
- U12 pad 7: Net-(R75-Pad2) -> Net-(R67-Pad2)
- U13 pad 11: Net-(R83-Pad2) -> Net-(R78-Pad2)
- U13 pad 13: Net-(R80-Pad2) -> Net-(R75-Pad2)
- U13 pad 14: Net-(R78-Pad2) -> Net-(R73-Pad2)
- U13 pad 15: Net-(R84-Pad2) -> Net-(R79-Pad2)
- U13 pad 16: Net-(R79-Pad2) -> Net-(R74-Pad2)
- U13 pad 3: Net-(R81-Pad2) -> Net-(R76-Pad2)
- U13 pad 4: Net-(Q15-Pad2) -> Net-(Q16-Pad2)
- U13 pad 5: Net-(R82-Pad2) -> Net-(R77-Pad2)
- U13 pad 7: Net-(R85-Pad2) -> Net-(R80-Pad2)
- U9 pad 1: Net-(R68-Pad1) -> Net-(R61-Pad1)
- U9 pad 15: Net-(R67-Pad1) -> Net-(R60-Pad1)
- U9 pad 2: Net-(R69-Pad1) -> Net-(R62-Pad1)
- U9 pad 3: Net-(R70-Pad1) -> Net-(R63-Pad1)
- U9 pad 4: Net-(R71-Pad1) -> Net-(R64-Pad1)
- U9 pad 5: Net-(R73-Pad1) -> Net-(R65-Pad1)
- U9 pad 6: Net-(R74-Pad1) -> Net-(R66-Pad1)
- U9 pad 7: Net-(R75-Pad1) -> Net-(R67-Pad1)
